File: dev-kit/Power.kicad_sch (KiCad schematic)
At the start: 20 parts, among them IC101 nPM1300-QEXX, X101 BATTERY

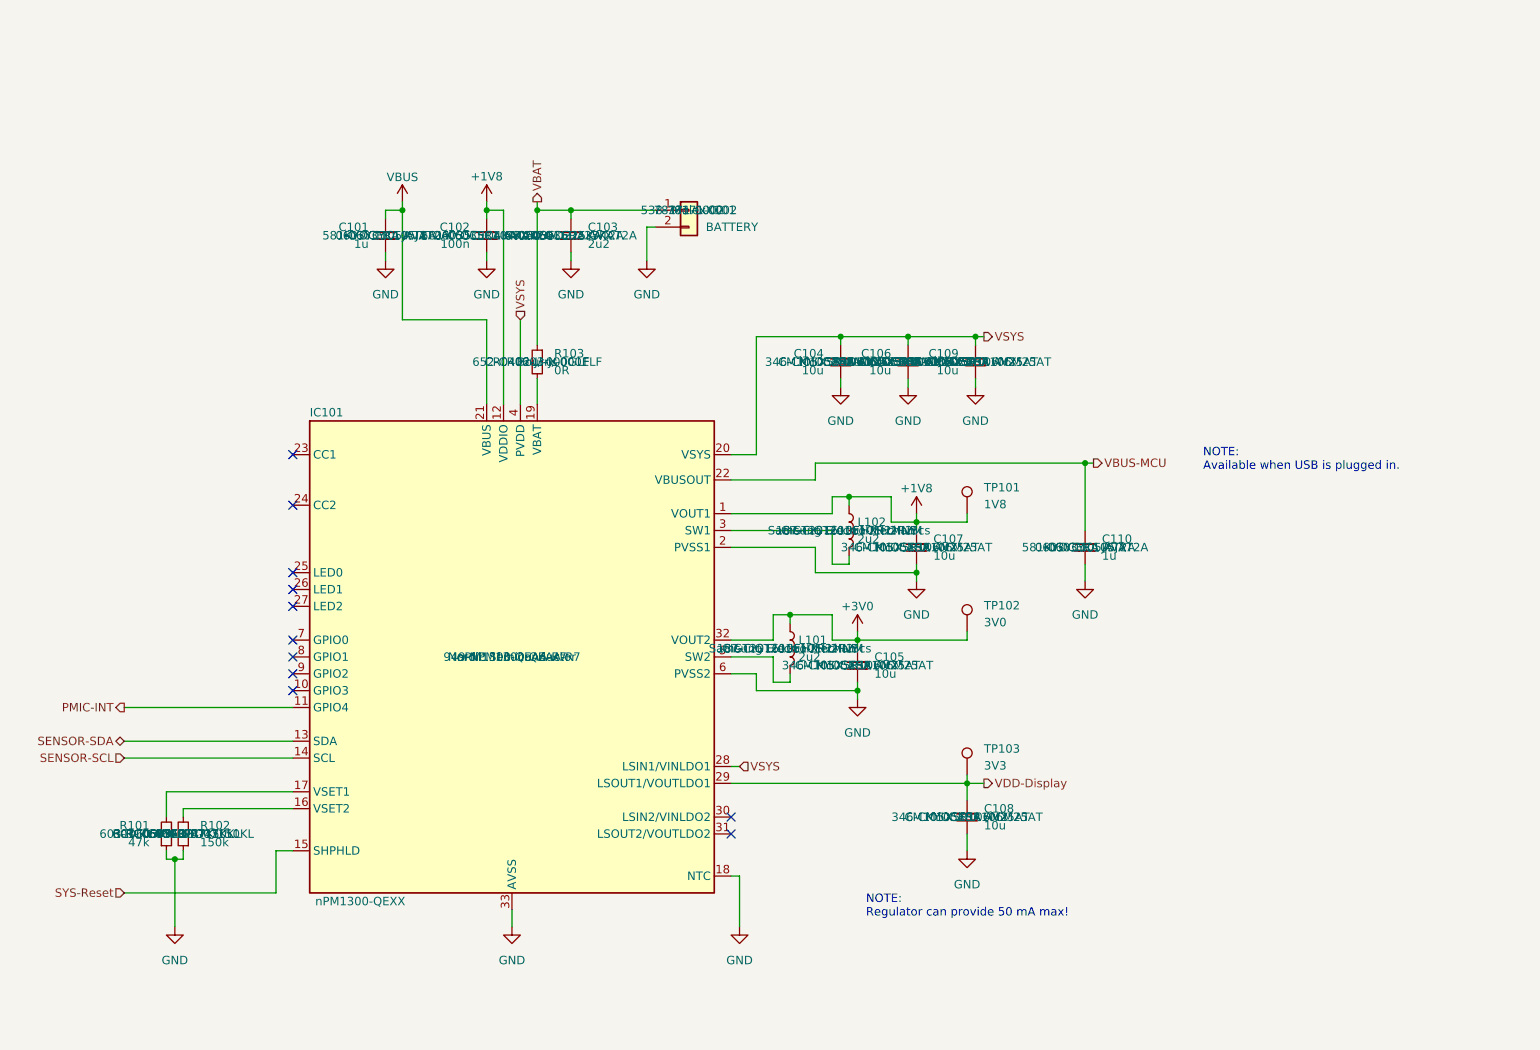
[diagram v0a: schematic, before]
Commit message: PCB: Add new vibration motor
- Remove old hardware project (comes back later)
- Add new dev-kit project

Closes #102

Signed-off-by: Daniel Kampert <danielkampert@kampis-elektroecke.de>
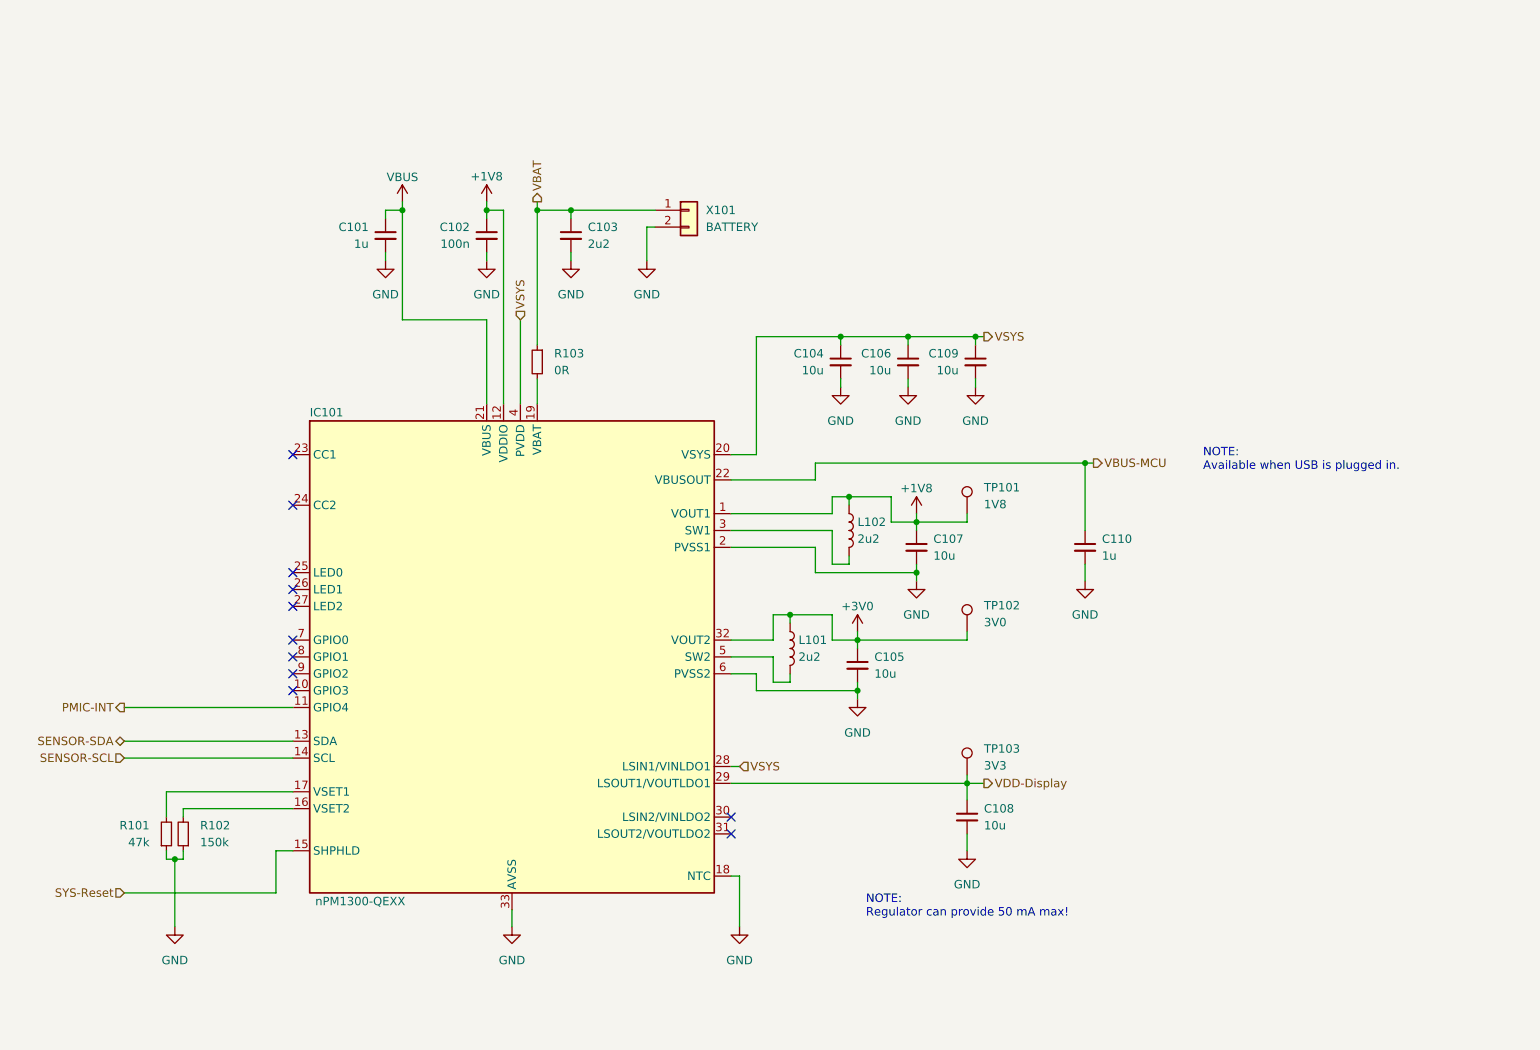
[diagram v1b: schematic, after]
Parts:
- C101, C102, C103, C104, C105, C106, C107, C108, C109, C110, IC101, L101, L102, R101, R102, R103, X101: Distributor Mouser -> (none)
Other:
- title: ZSWatch v3 -> ZSWatch v3 Dev-Kit

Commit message: Add 0805 resistors for current measurement, reorganize schematics
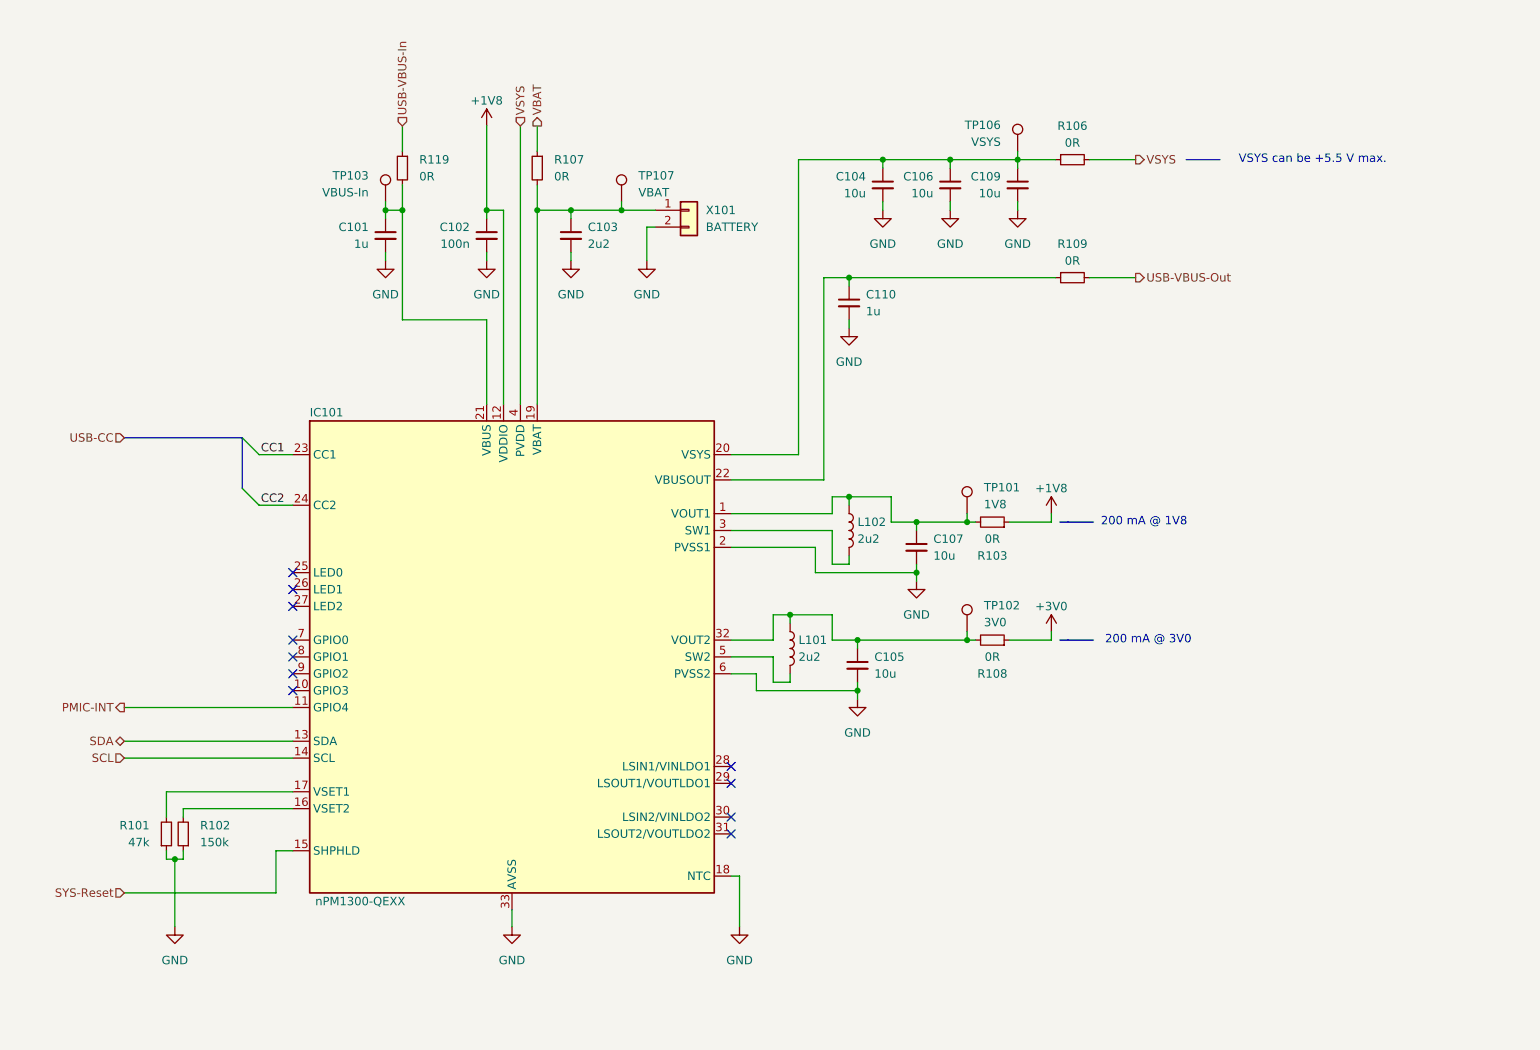
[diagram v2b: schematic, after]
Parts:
- removed C108: 10u, Capacitor_SMD:C_0603_1608Metric, symbol Device:C_Small
- added R106, R107, R108, R109, R119: 0R, Resistor_SMD:R_0805_2012Metric, symbol Device:R_Small
- added TP106: VSYS, TestPoint:TestPoint_Pad_D1.0mm, symbol Connector:TestPoint
- added TP107: VBAT, TestPoint:TestPoint_Pad_D1.0mm, symbol Connector:TestPoint
- C101, C110: footprint Capacitor_SMD:C_0603_1608Metric -> Capacitor_SMD:C_0402_1005Metric; manf# 0603YC105JAT2A -> 04023D105KAT2A; mouser# 581-0603YC105JAT2A -> 581-04023D105KAT2A
- C102: footprint Capacitor_SMD:C_0603_1608Metric -> Capacitor_SMD:C_0402_1005Metric; manf# 06035C104KAT2A -> 0402ZC104KAT4A; mouser# 581-06035C104KAT2A -> 581-0402ZC104KAT4A
- C103: footprint Capacitor_SMD:C_0603_1608Metric -> Capacitor_SMD:C_0402_1005Metric; manf# 06036D225KAT2A -> 04026D105MAT4A; mouser# 581-06036D225KAT2A -> 581-04026D105MAT4A
- C104, C105, C106, C107, C109: footprint Capacitor_SMD:C_0603_1608Metric -> Capacitor_SMD:C_0402_1005Metric; manf KYOCERA AVX -> Murata Electronics; manf# CM105X5R106M25AT -> GRJ155R60J106ME11D; mouser# 346-CM105X5R106M25AT -> 81-GRJ155R60J106ME11D
- L101, L102: footprint Inductor_SMD_Kampi:L_0806_2016 -> (none); manf Samsung Electro-Mechanics -> (none); manf# CIGT201610EH2R2MNE -> (none); mouser# 187-CIGT201610EH2R2M -> (none)
- R101: footprint Resistor_SMD:R_0603_1608Metric -> Resistor_SMD:R_0402_1005Metric; manf# RC0603FR-0747KL -> RC0402FR-0747KL; mouser# 603-RC0603FR-0747KL -> 603-RC0402FR-0747KL
- R102: footprint Resistor_SMD:R_0603_1608Metric -> Resistor_SMD:R_0402_1005Metric; manf# RC0603FR-07150KL -> RC0402FR-07150KL; mouser# 603-RC0603FR-07150KL -> 603-RC0402FR-07150KL
- R103: footprint Resistor_SMD:R_0402_1005Metric -> Resistor_SMD:R_0805_2012Metric; manf# CR0402-J/-000GLF -> CR0805-J/-000ELF; mouser# 652-CR0603-J/-000ELF -> 652-CR0805-J/-000ELF
- TP103: value 3V3 -> VBUS-In
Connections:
- net +1V8: now also R103.1; no longer C107.1, IC101.1 (VOUT1), L102.1, TP101.1
- net +3V0: now also R108.1; no longer C105.1, IC101.32 (VOUT2), L101.1, TP102.1
- net VBAT: now also R107.1; no longer C103.1, R103.1, X101.1 (Pin_1)
- net VSYS: now also R106.2; no longer C104.1, C106.1, C109.1, IC101.20 (VSYS), IC101.28 (LSIN1/VINLDO1)
- net at R103.2: now also C107.1, IC101.1 (VOUT1), L102.1, TP101.1; no longer IC101.19 (VBAT)
- net CC1: now reaches IC101.23 (CC1)
- net CC2: now reaches IC101.24 (CC2)
- net SENSOR-SCL renamed SCL
- net SENSOR-SDA renamed SDA
- net VBUS: no longer names the net of C101.1, IC101.21 (VBUS)
- net VBUS: now also TP103.1, R119.2
- net VBUS-MCU: no longer names the net of C110.1, IC101.22 (VBUSOUT)
- net VBUS-MCU: now also R109.1
- net VDD-Display: no longer names the net of IC101.29 (LSOUT1/VOUTLDO1)
- net VDD-Display: no longer TP103.1
- new net: C105.1, IC101.32 (VOUT2), L101.1, R108.2, TP102.1
- new net: C104.1, C106.1, C109.1, IC101.20 (VSYS), R106.1, TP106.1
- new net: C103.1, IC101.19 (VBAT), R107.2, TP107.1, X101.1 (Pin_1)
- new net USB-VBUS-In: R119.1
- new net USB-VBUS-Out: R109.2
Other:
- note added: "200 mA @ 1V8"
- note added: "200 mA @ 3V0"
- note added: "VSYS can be +5.5 V max."
- note removed: "NOTE: Available when USB is plugged in."
- note removed: "NOTE: Regulator can provide 50 mA max!"
- moved on the sheet: C104, C106, C109, C110, R103

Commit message: Working on the layout for the dev kit
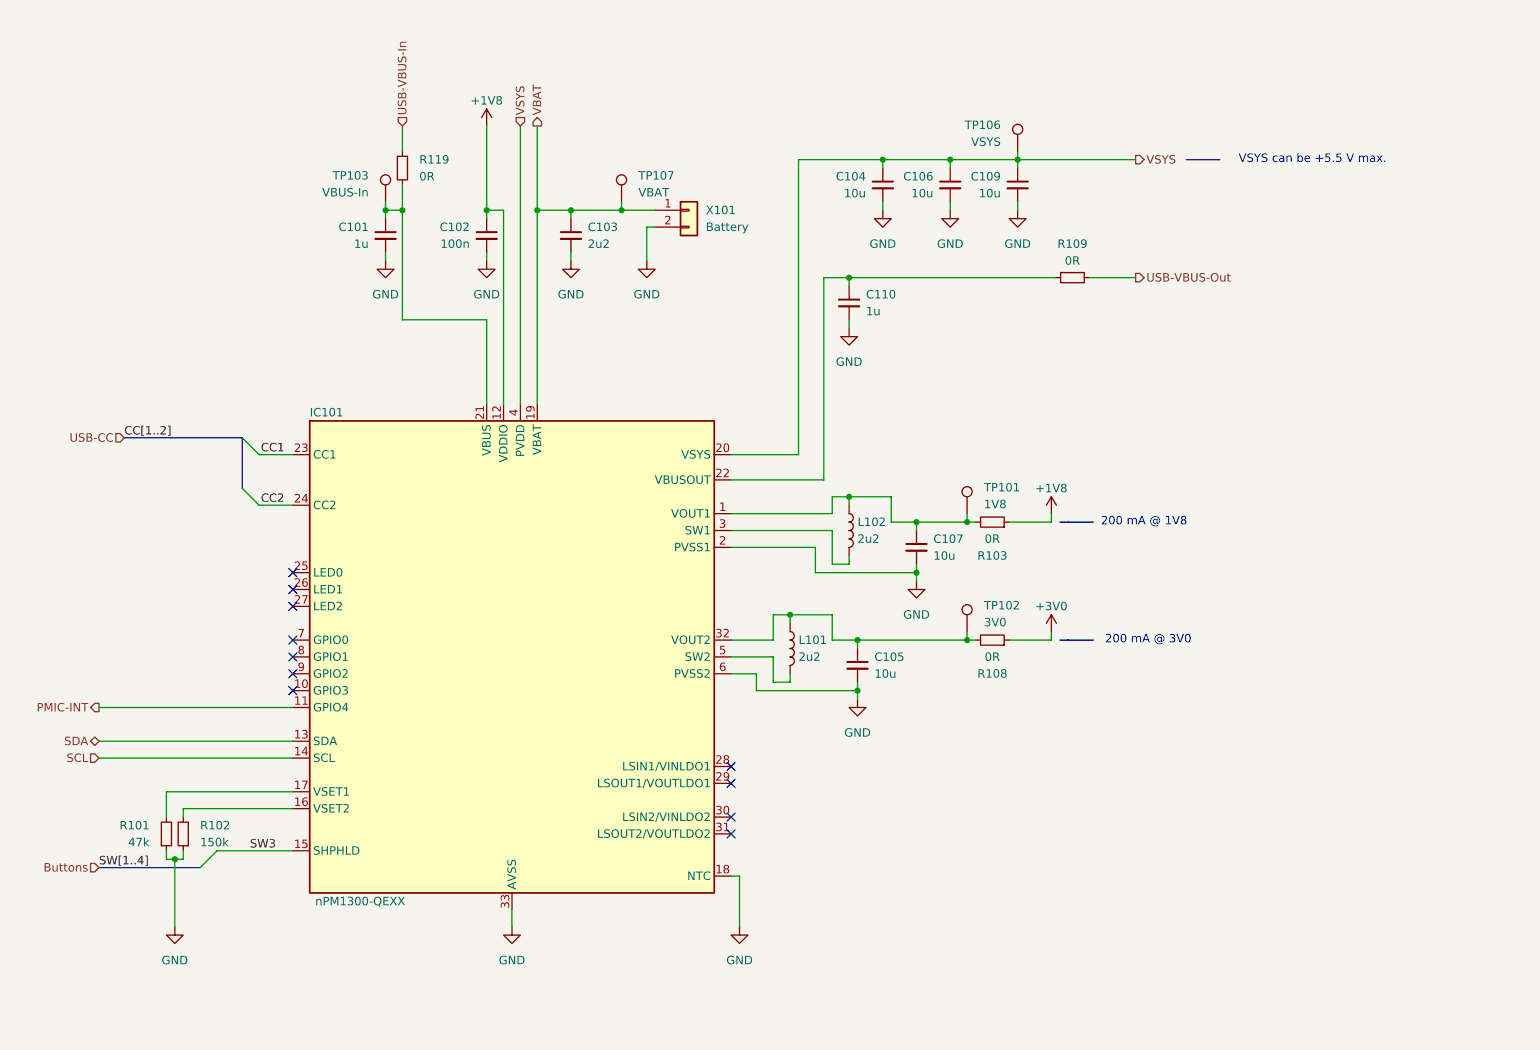
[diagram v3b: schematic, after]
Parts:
- removed R106, R107: 0R, Resistor_SMD:R_0805_2012Metric, symbol Device:R_Small
- C104, C106, C109: footprint Capacitor_SMD:C_0402_1005Metric -> Capacitor_SMD:C_0603_1608Metric; manf Murata Electronics -> KYOCERA AVX; manf# GRJ155R60J106ME11D -> KGM15CR50J106MT; mouser# 81-GRJ155R60J106ME11D -> 581-KGM15CR50J106MT
- L101, L102: footprint (none) -> Inductor_SMD_Kampi:L_0806_2016; manf (none) -> ABRACON; manf# (none) -> ASMPH-0806-2R2M-T; mouser# (none) -> 815-ASMPH-0806-2R2M-T
- X101: value BATTERY -> Battery
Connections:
- net VBAT: now also C103.1, IC101.19 (VBAT), TP107.1, X101.1 (Pin_1)
- net VSYS: now also C104.1, C106.1, C109.1, IC101.20 (VSYS), TP106.1
- net SYS-Reset renamed SW3

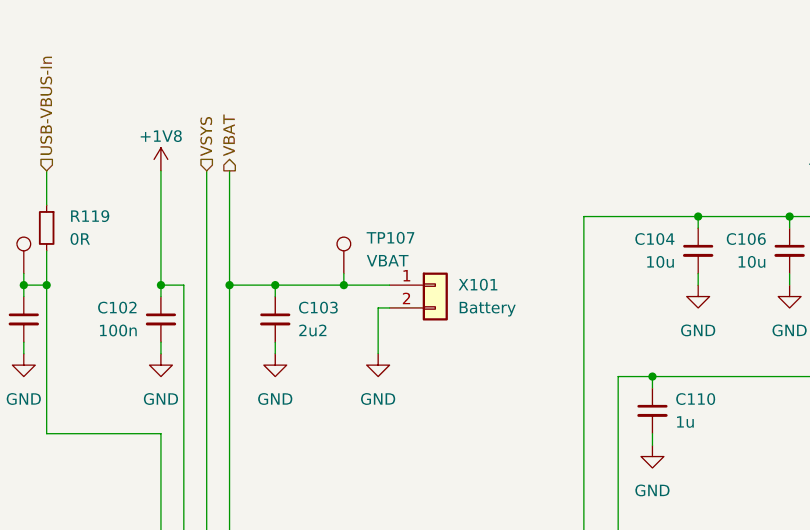
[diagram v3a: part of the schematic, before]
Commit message: PCB: Tweak silkscreen and headers.
- Added silkscreen labels to headers.
- Added function text to buttons.
- Made PCB 5mm wider (left) to make space for display (not sticking out of PCB) and allow more centered
buttons placement.
- Add header for UART pins (good in case we don't have a working dock built) (no mount).
- Changed from TP to header for VBAT for alternative way to connect battery (no mount).
- Added website url on silkscreen.
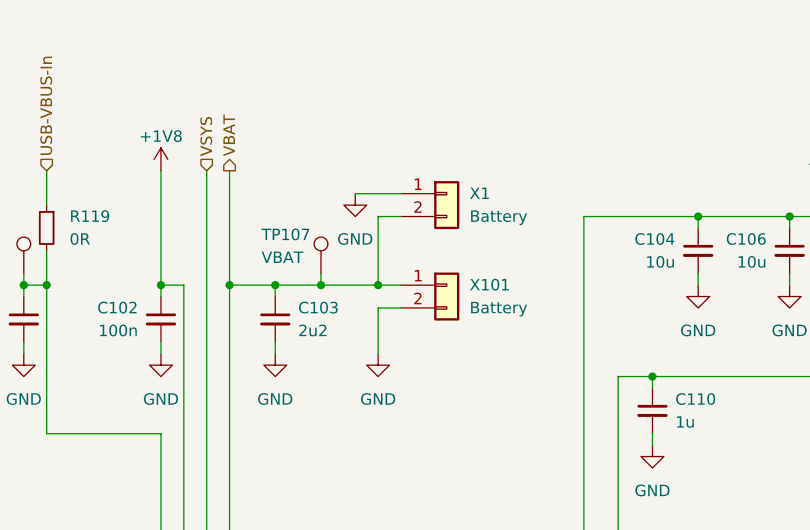
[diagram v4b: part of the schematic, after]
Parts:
- added X1: Battery, Connector_PinHeader_2.54mm:PinHeader_1x02_P2.54mm_Vertical, symbol Connector_Generic:Conn_01x02
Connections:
- net GND: now also X1.1 (Pin_1)
- net VBAT: now also X1.2 (Pin_2)
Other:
- moved on the sheet: TP107, X101

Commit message: Changes from Jacob
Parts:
- added X103: Power, Connector_PinHeader_2.54mm:PinHeader_1x04_P2.54mm_Vertical, symbol Connector_Generic:Conn_01x04
- renumbered C110 to C104, C104 to C106, C106 to C108, R119 to R103, R103 to R104, R108 to R105, R109 to R106, TP103 to TP101, TP107 to TP102, TP101 to TP103, TP102 to TP104, TP106 to TP105, X1 to X101, X101 to X102
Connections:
- net +1V8: now also X103.1 (Pin_1)
- net +3V0: now also X103.2 (Pin_2)
- net GND: now also X103.4 (Pin_4)
- net VSYS: now also X103.3 (Pin_3)
- net SW3 renamed SW2
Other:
- moved on the sheet: C101, R103, TP101

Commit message: Add impedance matching for USB, add jumper caps
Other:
- title: ZSWatch v3 Dev-Kit -> https://github.com/ZSWatch/Watch-HW
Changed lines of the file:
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@@
 	(paper "A4")
 	(title_block
-		(title "ZSWatch v3 Dev-Kit")
+		(title "https://github.com/ZSWatch/Watch-HW")
 		(date "2025-05-09")
 		(rev "0")

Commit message: Cosmetic changes
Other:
- company: github.com/jakkra/ZSWatch-HW -> https://github.com/ZSWatch/Watch-HW
- title: https://github.com/ZSWatch/Watch-HW -> Watch-HW
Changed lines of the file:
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@@
 	(paper "A4")
 	(title_block
-		(title "https://github.com/ZSWatch/Watch-HW")
+		(title "Watch-HW")
 		(date "2025-05-09")
 		(rev "0")
-		(company "github.com/jakkra/ZSWatch-HW")
+		(company "https://github.com/ZSWatch/Watch-HW")
 	)
 	(text "200 mA @ 1V8"
